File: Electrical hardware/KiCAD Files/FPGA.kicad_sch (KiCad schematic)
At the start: 2 parts, among them U1 ICE40UP5K-SG48ITR, Y1 ASV-xxxMHz

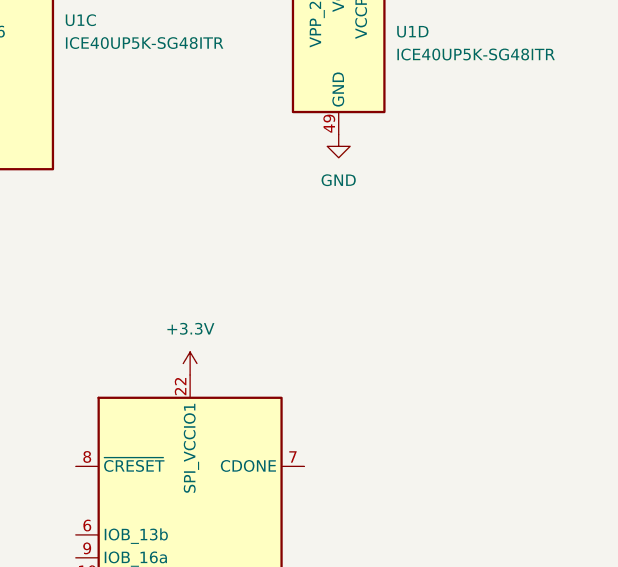
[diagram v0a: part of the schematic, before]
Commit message: adding voltage divider
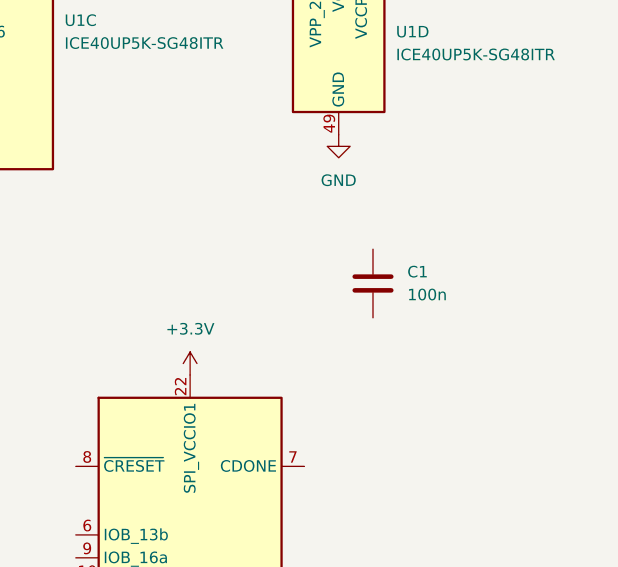
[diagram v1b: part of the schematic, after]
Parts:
- added C1: 100n, symbol Device:C
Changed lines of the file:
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@@
+	)
+	(symbol
+		(lib_id "Device:C")
+		(at 176.53 90.17 0)
+		(unit 1)
+		(exclude_from_sim no)
+		(in_bom yes)
+		(on_board yes)
+		(dnp no)
+		(fields_autoplaced yes)
+		(property "Reference" "C1"
+			(at 180.34 88.8999 0)
+			(effects
+				(font
+					(size 1.27 1.27)
+				)
+				(justify left)
+			)
+		)
+		(property "Value" "100n"
+			(at 180.34 91.4399 0)
+			(effects
+				(font
+					(size 1.27 1.27)
+				)
+				(justify left)
+			)
+		)
+		(property "Footprint" ""
+			(at 177.4952 93.98 0)
+			(effects
+				(font
+					(size 1.27 1.27)
+				)
+				(hide yes)
+			)
+		)
+		(property "Datasheet" "~"
+			(at 176.53 90.17 0)
+			(effects
+				(font
+					(size 1.27 1.27)
+				)
+				(hide yes)
+			)
+		)
+		(property "Description" "Unpolarized capacitor"
+			(at 176.53 90.17 0)
+			(effects
+				(font
+					(size 1.27 1.27)
+				)
+				(hide yes)
+			)
+		)
+		(pin "2"
+		)
+		(pin "1"
+		)
+		(instances
+			(project ""
+				(path "/6a8b9a9c-88ba-48a5-8033-e5e1453b50bb/ec80e5d1-e850-4436-a5fa-61773c455223"
+					(reference "C1")
+					(unit 1)
+				)
+			)
+		)
 	)
 	(symbol
